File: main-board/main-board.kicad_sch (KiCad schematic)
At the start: 89 parts, among them IC13 TPS2121RUXR, J47 Barrel Jack, J6 Conn_01x03, J66 Conn_01x01_Socket, J7 Conn_Boaxial, J73 Conn_01x03, J8 USB_C_Receptacle_USB2.0_16P, J9 Conn_02x04_Odd_Even, SW1 SW_Push, SW5 SW_Push, U10 SI5351A-B-GTR, U3 TLV75801PDBV, U5 TLV75801PDBV, X1 OK322532.768KJBA4SL, Y2 NX3225GA-25.000M-STD-CRG-2

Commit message: update testing board
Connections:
- net VDD_IO_main: no longer C24.1, C27.1, C44.1, D17.2 (A), R1.1, R12.1, R13.1, R30.2, R61.2, TP6.1, U10.7 (VDDO), U15.5 (+), U5.5 (OUT), X1.4 (Vcc)
- new net VDDIO: C24.1, C27.1, C44.1, D17.2 (A), R1.1, R12.1, R13.1, R30.2, R61.2, TP6.1, U10.7 (VDDO), U15.5 (+), U5.5 (OUT), X1.4 (Vcc)
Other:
- sheet chewing-gums ports: added none; removed A3V3_A, A3V3_B
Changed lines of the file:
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@@
 	)
 	(junction
-		(at 424.18 199.39)
-		(diameter 0)
-		(color 0 0 0 0)
-	)
-	(junction
 		(at 255.905 259.08)
 		(diameter 0)
@@
 	)
 	(bus_entry
-		(at 424.18 186.309)
-		(size 2.54 2.54)
-		(stroke
-			(width 0)
-			(type default)
-		)
-	)
-	(bus_entry
 		(at 492.125 106.68)
 		(size 2.54 -2.54)
@@
 	(wire
 		(pts
-			(xy 414.02 201.93) (xy 424.18 201.93)
-		)
-		(stroke
-			(width 0)
-			(type default)
-		)
-	)
-	(wire
-		(pts
 			(xy 414.02 345.44) (xy 415.29 345.44)
 		)
@@
 	(wire
 		(pts
-			(xy 424.18 196.85) (xy 424.18 199.39)
-		)
-		(stroke
-			(width 0)
-			(type default)
-		)
-	)
-	(wire
-		(pts
 			(xy 378.46 361.95) (xy 389.89 361.95)
 		)
@@
 	(wire
 		(pts
-			(xy 421.64 208.28) (xy 420.37 208.28)
-		)
-		(stroke
-			(width 0)
-			(type default)
-		)
-	)
-	(wire
-		(pts
 			(xy 375.285 272.415) (xy 385.445 272.415)
 		)
@@
 	(wire
 		(pts
-			(xy 414.02 207.264) (xy 421.64 207.264)
-		)
-		(stroke
-			(width 0)
-			(type default)
-		)
-	)
-	(wire
-		(pts
 			(xy 238.506 93.98) (xy 266.7 93.98)
 		)
@@
 		)
 	)
-	(wire
-		(pts
-			(xy 421.64 207.264) (xy 421.64 208.28)
-		)
-		(stroke
-			(width 0)
-			(type default)
-		)
-	)
 	(polyline
 		(pts
@@
 	(bus
 		(pts
-			(xy 424.18 186.309) (xy 424.18 192.024)
-		)
-		(stroke
-			(width 0)
-			(type default)
-		)
-	)
-	(bus
-		(pts
 			(xy 456.565 287.655) (xy 456.565 290.195)
 		)
@@
 	(wire
 		(pts
-			(xy 414.02 209.804) (xy 420.37 209.804)
+			(xy 414.02 208.28) (xy 416.56 208.28)
 		)
 		(stroke
@@
 	(bus
 		(pts
-			(xy 424.18 178.689) (xy 424.18 186.309)
+			(xy 424.18 178.689) (xy 424.18 194.31)
 		)
 		(stroke
@@
 	(wire
 		(pts
-			(xy 420.37 209.804) (xy 420.37 210.82)
-		)
-		(stroke
-			(width 0)
-			(type default)
-		)
-	)
-	(wire
-		(pts
 			(xy 415.29 351.79) (xy 415.29 345.44)
 		)
@@
 	(wire
 		(pts
-			(xy 414.02 196.85) (xy 424.18 196.85)
-		)
-		(stroke
-			(width 0)
-			(type default)
-		)
-	)
-	(wire
-		(pts
 			(xy 323.85 140.335) (xy 334.01 140.335)
 		)
@@
 		)
 	)
+	(wire
+		(pts
+			(xy 414.02 205.74) (xy 416.56 205.74)
+		)
+		(stroke
+			(width 0)
+			(type default)
+		)
+	)
 	(polyline
 		(pts
@@
 	(bus
 		(pts
-			(xy 414.02 192.024) (xy 424.18 192.024)
+			(xy 414.02 194.31) (xy 424.18 194.31)
 		)
 		(stroke
@@
 		)
 	)
-	(wire
-		(pts
-			(xy 424.18 199.39) (xy 429.26 199.39)
-		)
-		(stroke
-			(width 0)
-			(type default)
-		)
-	)
 	(bus
 		(pts
@@
 	(wire
 		(pts
-			(xy 424.18 201.93) (xy 424.18 199.39)
-		)
-		(stroke
-			(width 0)
-			(type default)
-		)
-	)
-	(wire
-		(pts
 			(xy 306.07 251.46) (xy 314.96 251.46)
 		)
@@
 	(wire
 		(pts
-			(xy 426.72 188.849) (xy 436.88 188.849)
-		)
-		(stroke
-			(width 0)
-			(type default)
-		)
-	)
-	(wire
-		(pts
 			(xy 114.3 260.35) (xy 118.11 260.35)
 		)
@@
 		)
 	)
-	(label "VDD_IO_main"
+	(label "VDDIO"
 		(at 493.395 174.625 180)
 		(effects
@@
 	)
 	(label "REF_B"
-		(at 420.37 210.82 0)
+		(at 416.56 208.28 0)
 		(effects
 			(font
@@
 		)
 	)
-	(label "VDD_IO_main"
+	(label "VDDIO"
 		(at 502.285 276.86 0)
 		(effects
@@
 		)
 	)
-	(label "VDD_IO_main"
+	(label "VDDIO"
 		(at 371.475 100.965 0)
 		(effects
@@
 		)
 	)
-	(label "VDD_IO_main"
+	(label "VDDIO"
 		(at 78.74 280.67 0)
 		(effects
@@
 		)
 	)
-	(label "Vout_A_6"
-		(at 435.61 188.849 180)
-		(effects
-			(font
-				(size 1.27 1.27)
-			)
-			(justify right bottom)
-		)
-	)
 	(label "EN_CG_10"
 		(at 375.285 292.735 0)
@@
 	)
 	(label "REF_A"
-		(at 420.37 208.28 0)
+		(at 416.56 205.74 0)
 		(effects
 			(font
@@
 		)
 	)
-	(label "VDD_IO_main"
+	(label "VDDIO"
 		(at 102.87 247.015 0)
 		(effects
@@
 		)
 	)
-	(global_label "3V3"
-		(shape input)
-		(at 429.26 199.39 0)
-		(fields_autoplaced yes)
-		(effects
-			(font
-				(size 3 3)
-			)
-			(justify left)
-		)
-		(property "Intersheetrefs" "${INTERSHEET_REFS}"
-			(at 444.5959 199.39 0)
-			(effects
-				(font
-					(size 1.27 1.27)
-				)
-				(justify left)
-				(hide yes)
-			)
-		)
-	)
-	(global_label "VDD_IO_cheep"
-		(shape input)
-		(at 436.88 188.849 0)
-		(fields_autoplaced yes)
-		(effects
-			(font
-				(size 2 2)
-			)
-			(justify left)
-		)
-		(property "Intersheetrefs" "${INTERSHEET_REFS}"
-			(at 462.1517 188.849 0)
-			(effects
-				(font
-					(size 1.27 1.27)
-				)
-				(justify left)
-				(hide yes)
-			)
-		)
-	)
 	(global_label "SCL"
 		(shape input)
@@
 		)
 	)
-	(global_label "VDD_IO_main"
+	(global_label "VDDIO"
 		(shape input)
 		(at 330.2 325.12 0)
@@
 		)
 		(property "Intersheetrefs" "${INTERSHEET_REFS}"
-			(at 353.9479 325.12 0)
+			(at 343.6622 325.12 0)
 			(effects
 				(font
@@
 			)
 		)
-		(pin "A3V3_A" output
-			(at 414.02 196.85 0)
-			(effects
-				(font
-					(size 1.27 1.27)
-				)
-				(justify right)
-			)
-		)
 		(pin "REF_A" output
-			(at 414.02 207.264 0)
+			(at 414.02 205.74 0)
 			(effects
 				(font
@@
 		)
 		(pin "REF_B" output
-			(at 414.02 209.804 0)
-			(effects
-				(font
-					(size 1.27 1.27)
-				)
-				(justify right)
-			)
-		)
-		(pin "A3V3_B" output
-			(at 414.02 201.93 0)
+			(at 414.02 208.28 0)
 			(effects
 				(font
@@
 		)
 		(pin "Vout_A_[1..12]" output
-			(at 414.02 192.024 0)
+			(at 414.02 194.31 0)
 			(effects
 				(font

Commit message: pcb update
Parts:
- TP1, TP2, TP3, TP4, TP5, TP6: footprint Library:TP_50_28_RING -> TestPoint:TestPoint_Loop_D1.80mm_Drill1.0mm_Beaded
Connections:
- net -5V: now also TP1.1
- net GND: no longer TP1.1
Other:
- moved on the sheet: TP1
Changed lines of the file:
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@@
 	)
 	(junction
-		(at 434.34 361.95)
-		(diameter 0)
-		(color 0 0 0 0)
-	)
-	(junction
 		(at 217.17 341.63)
 		(diameter 0)
@@
 	)
 	(junction
+		(at 412.75 384.81)
+		(diameter 0)
+		(color 0 0 0 0)
+	)
+	(junction
 		(at 86.995 250.825)
 		(diameter 0)
@@
 	(wire
 		(pts
-			(xy 433.07 361.95) (xy 434.34 361.95)
-		)
-		(stroke
-			(width 0)
-			(type default)
-		)
-	)
-	(wire
-		(pts
-			(xy 434.34 361.95) (xy 444.5 361.95)
+			(xy 433.07 361.95) (xy 444.5 361.95)
 		)
 		(stroke
@@
 	(wire
 		(pts
+			(xy 412.75 384.81) (xy 426.72 384.81)
+		)
+		(stroke
+			(width 0)
+			(type default)
+		)
+	)
+	(wire
+		(pts
 			(xy 267.97 259.08) (xy 255.905 259.08)
 		)
@@
 	(wire
 		(pts
-			(xy 405.13 384.81) (xy 426.72 384.81)
+			(xy 405.13 384.81) (xy 412.75 384.81)
 		)
 		(stroke
@@
 			)
 		)
-		(property "Footprint" "Library:TP_50_28_RING"
+		(property "Footprint" "TestPoint:TestPoint_Loop_D1.80mm_Drill1.0mm_Beaded"
 			(at 281.8892 268.8082 0)
 			(effects
@@
 			)
 		)
-		(property "Footprint" "Library:TP_50_28_RING"
+		(property "Footprint" "TestPoint:TestPoint_Loop_D1.80mm_Drill1.0mm_Beaded"
 			(at 297.1292 334.4418 0)
 			(effects
@@
 			)
 		)
-		(property "Footprint" "Library:TP_50_28_RING"
+		(property "Footprint" "TestPoint:TestPoint_Loop_D1.80mm_Drill1.0mm_Beaded"
 			(at 306.0192 298.8818 0)
 			(effects
@@
 			)
 		)
-		(property "Footprint" "Library:TP_50_28_RING"
+		(property "Footprint" "TestPoint:TestPoint_Loop_D1.80mm_Drill1.0mm_Beaded"
 			(at 266.6492 241.7318 0)
 			(effects
@@
 	(symbol
 		(lib_id "Library:TP")
-		(at 434.34 361.95 0)
+		(at 412.75 384.81 0)
 		(unit 1)
 		(exclude_from_sim no)
@@
 		(fields_autoplaced yes)
 		(property "Reference" "TP1"
-			(at 443.23 359.6871 0)
+			(at 421.64 382.5471 0)
 			(effects
 				(font
@@
 		)
 		(property "Value" "~"
-			(at 443.23 361.5921 0)
+			(at 421.64 384.4521 0)
 			(effects
 				(font
@@
 			)
 		)
-		(property "Footprint" "Library:TP_50_28_RING"
-			(at 434.2892 364.9218 0)
+		(property "Footprint" "TestPoint:TestPoint_Loop_D1.80mm_Drill1.0mm_Beaded"
+			(at 412.6992 387.7818 0)
 			(effects
 				(font
@@
 		)
 		(property "Datasheet" ""
-			(at 434.34 361.95 0)
+			(at 412.75 384.81 0)
 			(effects
 				(font
@@
 		)
 		(property "Description" ""
-			(at 434.34 361.95 0)
+			(at 412.75 384.81 0)
 			(effects
 				(font
@@
 			)
 		)
-		(property "Footprint" "Library:TP_50_28_RING"
+		(property "Footprint" "TestPoint:TestPoint_Loop_D1.80mm_Drill1.0mm_Beaded"
 			(at 314.9092 241.7318 0)
 			(effects

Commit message: pcb update
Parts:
- added J2: Conn_01x01_Socket, Connector:Banana_Jack_1Pin, symbol Connector:Conn_01x01_Socket
- added R74, R75: 1k, Resistor_SMD:R_0603_1608Metric, symbol Device:R
- J9: footprint (none) -> Connector_PinHeader_2.54mm:PinHeader_2x04_P2.54mm_Vertical_SMD
- L3: footprint (none) -> Inductor_SMD:L_Coilcraft_XAL5030-XXX
- RV1: footprint (none) -> Potentiometer_THT:Potentiometer_Bourns_3296W_Vertical
- U4: value ~ -> MAX17577; footprint (none) -> Package_DFN_QFN:DFN-12-1EP_3x3mm_P0.45mm_EP1.65x2.38mm_ThermalVias
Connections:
- net VDD_IO_main is gone; now on net VDDIO: R14.2
- net -5V: now also U4.13 (EP); no longer U4.EP
- net 3V3: now also R12.1, R13.1
- net 5V: now also C41.1, C42.1, R51.1, U4.1 (IN)
- net GND: now also C41.2, C42.2, U4.9 (GND), J2.1 (Pin_1), R74.2; no longer U15.6 (-)
- net VDDIO: now also R75.2; no longer R12.1, R13.1, U15.5 (+)
- net at R68.1: now also J9.3 (Pin_3); no longer J9.5 (Pin_5)
- net LX: now reaches C29.2, L3.1, U4.11 (LX)
- net at J9.1 (Pin_1): now also RV1.1; no longer R62.1
- net at R67.1: now also J9.5 (Pin_5); no longer J9.3 (Pin_3)
- net at J9.7 (Pin_7): now also R62.1; no longer RV1.1
- new net: R75.1, U15.5 (+)
- new net: R74.1, U15.6 (-)
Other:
- sheet I2C_expander ports: added SCL_CHEEP, SDA_CHEEP; removed ADCDAC_I2C_SCL_LEFT, ADCDAC_I2C_SCL_RIGHT, ADCDAC_I2C_SDA_LEFT, ADCDAC_I2C_SDA_RIGHT
- sheet chewing-gums ports: added none; removed ADCDAC_I2C_SCL_LEFT, ADCDAC_I2C_SCL_RIGHT, ADCDAC_I2C_SDA_LEFT, ADCDAC_I2C_SDA_RIGHT
- moved on the sheet: J9, R12, R13, U15

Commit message: PCB update
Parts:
- removed R12, R13: 10k, Resistor_SMD:R_0603_1608Metric, symbol Device:R_Small
- added D18: LED, LED_SMD:LED_0603_1608Metric, symbol Device:LED
- added R78: 2k, Resistor_SMD:R_0603_1608Metric, symbol Device:R
- C17, C19, C60: value 1u -> 1uF
- C20, C43: value 10u -> 10uF
- C22, C44: value 22u -> 22uF; LCSC (none) -> C59461
- C23, C25: value 1p -> 1pF
- C24, C26, C27: value 0.1u -> 100nF; LCSC C19702 -> C30926
- C29: value 0.1u -> 100nF; LCSC (none) -> C30926
- C30: LCSC (none) -> C59461
- C39: LCSC (none) -> C1607
- C40: LCSC (none) -> C1628
- C41, C42: LCSC (none) -> C19666
- C59: value 100n -> 100nF; LCSC (none) -> C30926
- C61: value 100u -> 100uF; LCSC C111600 -> C7469933
- D13, D14: LCSC (none) -> C552530
- J6: LCSC (none) -> C41417342
- J7: LCSC (none) -> C2987686
- J73: LCSC (none) -> C5116529
- J8: LCSC (none) -> C5184243
- J9: LCSC (none) -> C192300
- L3: LCSC (none) -> C3911698
- R15, R66: LCSC (none) -> C21190
- R28, R29: value 1k -> 2k; LCSC C21190 -> C22975
- R4, R5, R70, R71: LCSC (none) -> C1203
- R43, R44: LCSC C98220 -> C23186
- R46, R61: LCSC (none) -> C25803
- R47, R62, R69: LCSC (none) -> C4184
- R48: LCSC C98220 -> C23196
- R49: LCSC C98220 -> C33619
- R50: LCSC C98220 -> C23184
- R51: LCSC C98220 -> C327396
- R52: LCSC C98220 -> C482628
- R54, R55: LCSC (none) -> C22843
- R56: LCSC C98220 -> C23085
- R57, R59: LCSC (none) -> C22912
- R58, R60: value 5k1 -> 5.1k; LCSC (none) -> C23186
- R67: LCSC (none) -> C844365
- R68: LCSC (none) -> C23121
- RV1: LCSC (none) -> C83694
- SW1, SW5: LCSC (none) -> C221678
- U10: LCSC C1985619 -> C504891
- U15: value ~ -> BIWIN_DTS04GE_SMD; LCSC (none) -> C3294670; lcsc (none) -> C3294670
- U4: LCSC (none) -> C2930958
- X1: LCSC (none) -> C725996
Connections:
- net 3V3: now also R30.2
- net GND: now also D18.1 (K)
- net VDDIO: no longer R30.2
- new net: D18.2 (A), R78.2
- new net LED_FTDI_3: R78.1
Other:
- sheet I2C_expander ports: added none; removed SCL_RIGHT, SDA_RIGHT
- sheet IO-expander ports: added GPIO_[5..20], LED_FTDI_3; removed GPIO_[5..17]
- moved on the sheet: D10, D12, R28, R30, R59, SW1

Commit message: Testing board final version & production data
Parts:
- added TP10, TP11, TP12, TP13, TP14, TP7, TP8, TP9: 5029, TestPoint:TestPoint_Keystone_5019_Miniature, symbol dk_Test-Points:5029
- IC13: footprint SOTFL50P160X60-8N -> heep_footprints:TI-VQFN-HR-12
- J47: symbol Connector:Barrel_Jack_MountingPin -> Connector:Barrel_Jack
- L3: footprint Inductor_SMD:L_Coilcraft_XAL5030-XXX -> Inductor_SMD:L_Vishay_IHLP-2020
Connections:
- net GND: now also TP10.1, TP11.1, TP12.1, TP13.1, TP14.1, TP7.1, TP8.1, TP9.1
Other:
- sheet GPIO_playground ports: added HEEP_RESET; removed none

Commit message: production files
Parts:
- J6: LCSC C41417342 -> C5160786
- L3: LCSC C3911698 -> C844996
- U4: footprint Package_DFN_QFN:DFN-12-1EP_3x3mm_P0.45mm_EP1.65x2.38mm_ThermalVias -> heep_footprints:MAX17577-12-TDFN-EP
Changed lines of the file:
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@@
 			)
 		)
-		(property "LCSC" "C3911698"
+		(property "LCSC" "C844996"
 			(at 421.64 359.664 0)
 			(effects
@@
 			)
 		)
-		(property "LCSC" "C41417342"
+		(property "LCSC" "C5160786"
 			(at 65.786 302.641 0)
 			(effects
@@
 			)
 		)
-		(property "Footprint" "Package_DFN_QFN:DFN-12-1EP_3x3mm_P0.45mm_EP1.65x2.38mm_ThermalVias"
+		(property "Footprint" "heep_footprints:MAX17577-12-TDFN-EP"
 			(at 401.32 364.49 0)
 			(effects

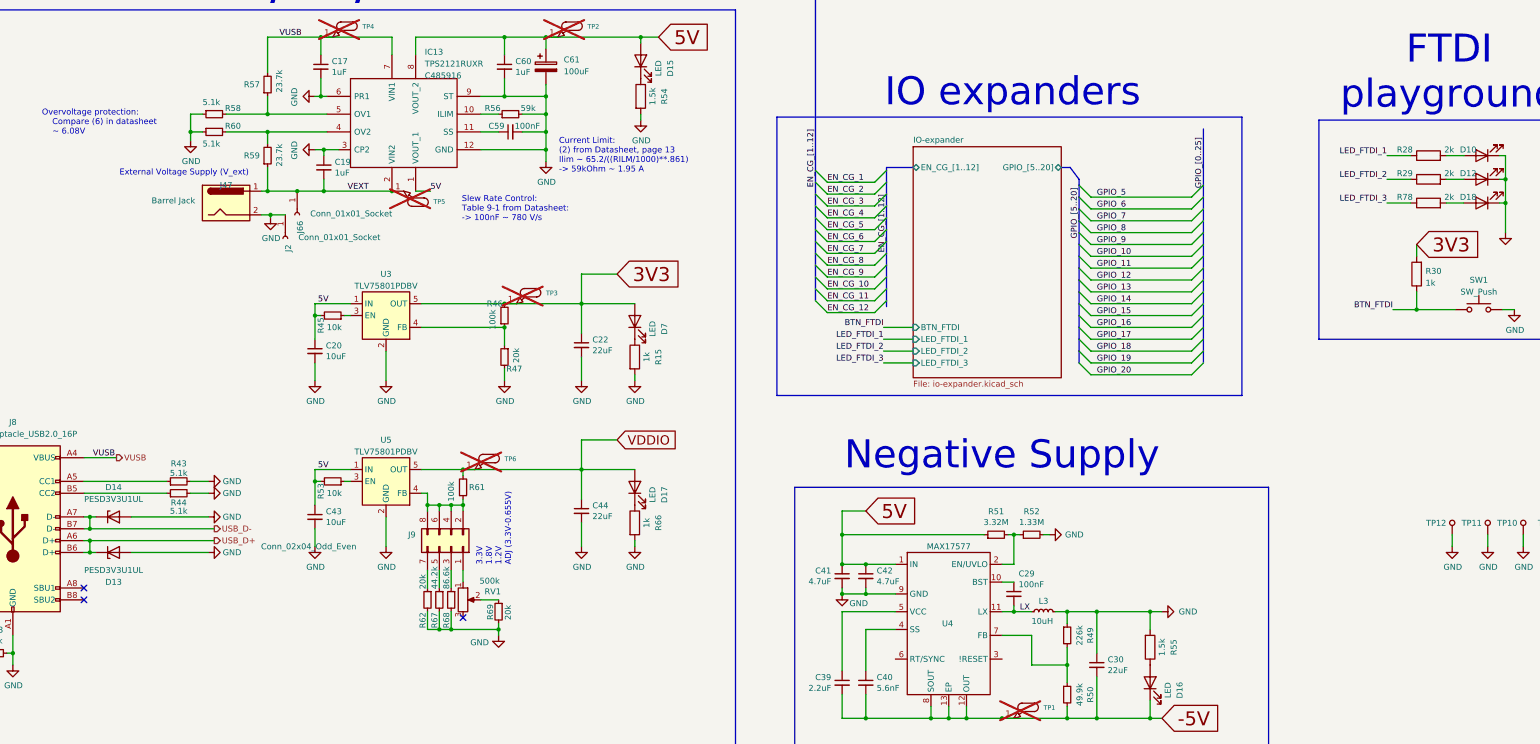
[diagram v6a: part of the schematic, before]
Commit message: 🪲🔫 Fixed bugs on polarities
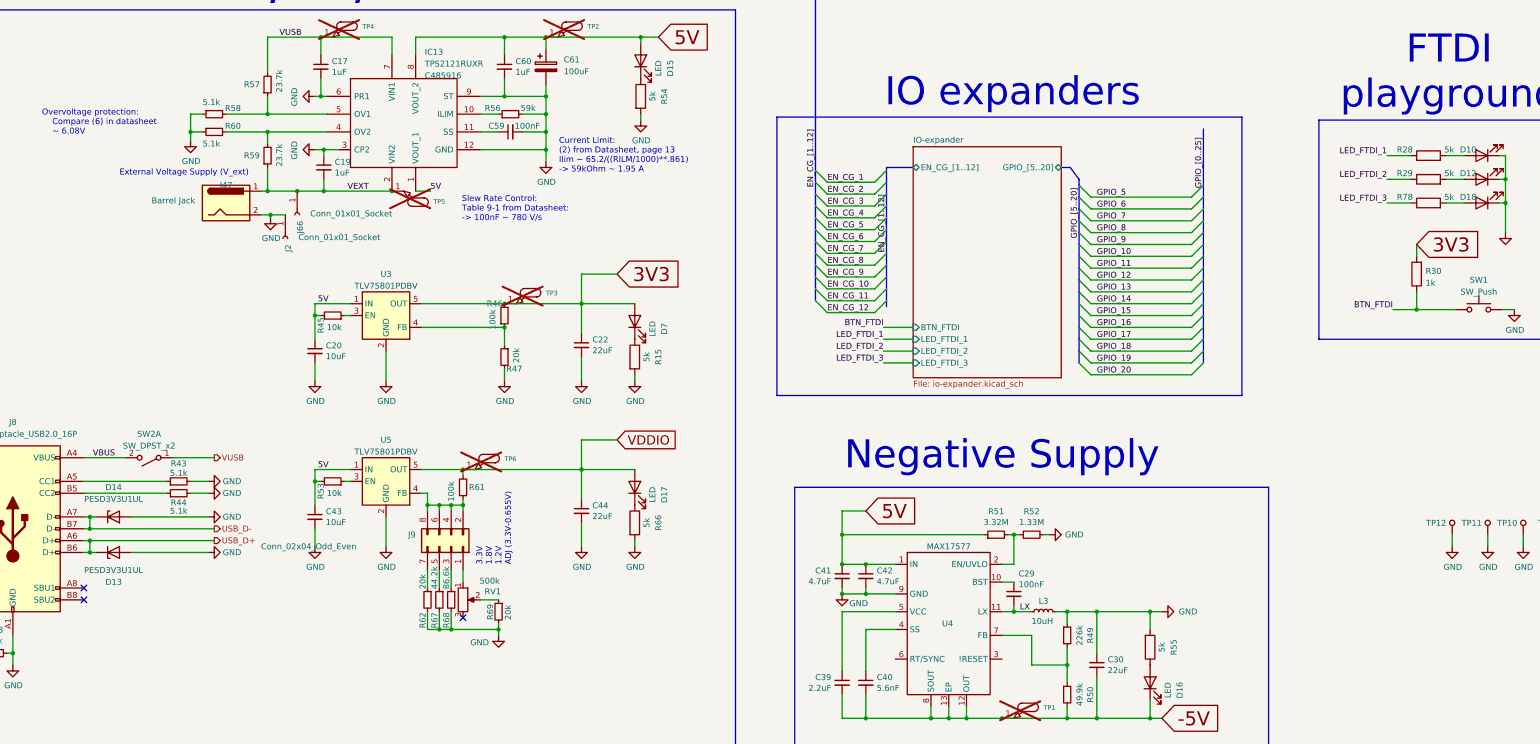
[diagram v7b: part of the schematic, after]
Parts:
- added SW2: SW_DPST_x2, Library:SW_TE_1825255-1, symbol Switch:SW_DPST_x2
- R15, R66: value 1k -> 5k
- R28, R29, R78: value 2k -> 5k
- R54, R55: value 1.5k -> 5k
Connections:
- net VUSB: now also SW2.1 (A); no longer J8.A4 (VBUS), J8.A9 (VBUS), J8.B4 (VBUS), J8.B9 (VBUS)
- new net VBUS: J8.A4 (VBUS), J8.A9 (VBUS), J8.B4 (VBUS), J8.B9 (VBUS), SW2.2 (B)
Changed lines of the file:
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@@
 	(wire
 		(pts
-			(xy 215.9 328.93) (xy 222.885 328.93)
+			(xy 215.9 328.93) (xy 224.79 328.93)
 		)
 		(stroke
@@
 	(wire
 		(pts
+			(xy 234.95 328.93) (xy 243.84 328.93)
+		)
+		(stroke
+			(width 0)
+			(type default)
+		)
+	)
+	(wire
+		(pts
 			(xy 419.1 373.38) (xy 426.72 373.38)
 		)
@@
 		)
 	)
-	(label "VUSB"
+	(label "VBUS"
 		(at 217.805 328.93 0)
 		(effects
@@
 	(hierarchical_label "VUSB"
 		(shape output)
-		(at 222.885 328.93 0)
+		(at 243.84 328.93 0)
 		(effects
 			(font
@@
 			)
 		)
-		(property "Value" "2k"
+		(property "Value" "5k"
 			(at 508.635 262.89 90)
 			(effects
@@
 	)
 	(symbol
+		(lib_id "Switch:SW_DPST_x2")
+		(at 229.87 328.93 180)
+		(unit 1)
+		(exclude_from_sim no)
+		(in_bom yes)
+		(on_board yes)
+		(dnp no)
+		(fields_autoplaced yes)
+		(property "Reference" "SW2"
+			(at 229.87 323.85 0)
+			(effects
+				(font
+					(size 1.27 1.27)
+				)
+			)
+		)
+		(property "Value" "SW_DPST_x2"
+			(at 229.87 326.39 0)
+			(effects
+				(font
+					(size 1.27 1.27)
+				)
+			)
+		)
+		(property "Footprint" "Library:SW_TE_1825255-1"
+			(at 229.87 328.93 0)
+			(effects
+				(font
+					(size 1.27 1.27)
+				)
+				(hide yes)
+			)
+		)
+		(property "Datasheet" "~"
+			(at 229.87 328.93 0)
+			(effects
+				(font
+					(size 1.27 1.27)
+				)
+				(hide yes)
+			)
+		)
+		(property "Description" "Single Pole Single Throw (SPST) switch, separate symbol"
+			(at 229.87 328.93 0)
+			(effects
+				(font
+					(size 1.27 1.27)
+				)
+				(hide yes)
+			)
+		)
+		(pin "2"
+		)
+		(pin "3"
+		)
+		(pin "4"
+		)
+		(pin "1"
+		)
+		(instances
+			(project ""
+				(path "/6198f783-b154-4adf-87fa-b1d9cb913fe2"
+					(reference "SW2")
+					(unit 1)
+				)
+			)
+		)
+	)
+	(symbol
 		(lib_id "Connector:USB_C_Receptacle_USB2.0_16P")
 		(at 200.66 344.17 0)
@@
 			)
 		)
-		(property "Value" "1k"
+		(property "Value" "5k"
 			(at 336.55 307.34 90)
 			(effects
@@
 			)
 		)
-		(property "Value" "2k"
+		(property "Value" "5k"
 			(at 508.635 267.97 90)
 			(effects
@@
 			)
 		)
-		(property "Value" "1.5k"
+		(property "Value" "5k"
 			(at 447.04 369.57 90)
 			(effects
@@
 			)
 		)
-		(property "Value" "2k"
+		(property "Value" "5k"
 			(at 508.635 273.05 90)
 			(effects
@@
 			)
 		)
-		(property "Value" "1.5k"
+		(property "Value" "5k"
 			(at 337.82 251.46 90)
 			(effects
@@
 			)
 		)
-		(property "Value" "1k"
+		(property "Value" "5k"
 			(at 336.55 342.9 90)
 			(effects

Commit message: Reflected changes on sch
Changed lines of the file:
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@@
+		)
+	)
+	(global_label "VUSB"
+		(shape input)
+		(at 243.84 328.93 0)
+		(fields_autoplaced yes)
+		(effects
+			(font
+				(size 2 2)
+			)
+			(justify left)
+		)
+		(property "Intersheetrefs" "${INTERSHEET_REFS}"
+			(at 256.2546 328.93 0)
+			(effects
+				(font
+					(size 1.27 1.27)
+				)
+				(justify left)
+				(hide yes)
+			)
 		)
 	)
@@
 		(effects
 			(font
-				(size 1.27 1.27)
-			)
-			(justify left)
-		)
-	)
-	(hierarchical_label "VUSB"
-		(shape output)
-		(at 243.84 328.93 0)
-		(effects
-			(font
